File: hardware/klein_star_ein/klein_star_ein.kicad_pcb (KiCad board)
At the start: 2 copper layers, 1 part, among them U1 MT41K512M16

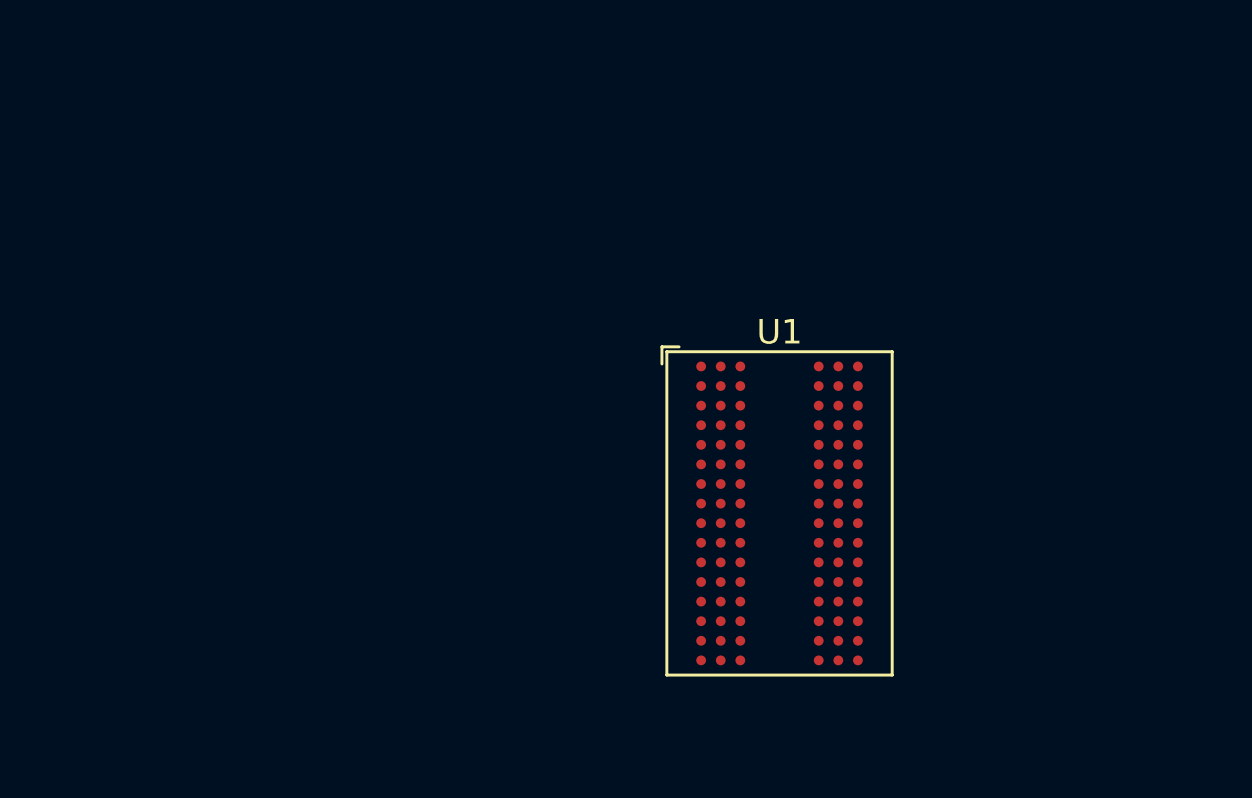
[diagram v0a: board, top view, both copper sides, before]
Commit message: fixed DRAM, added initial schematic
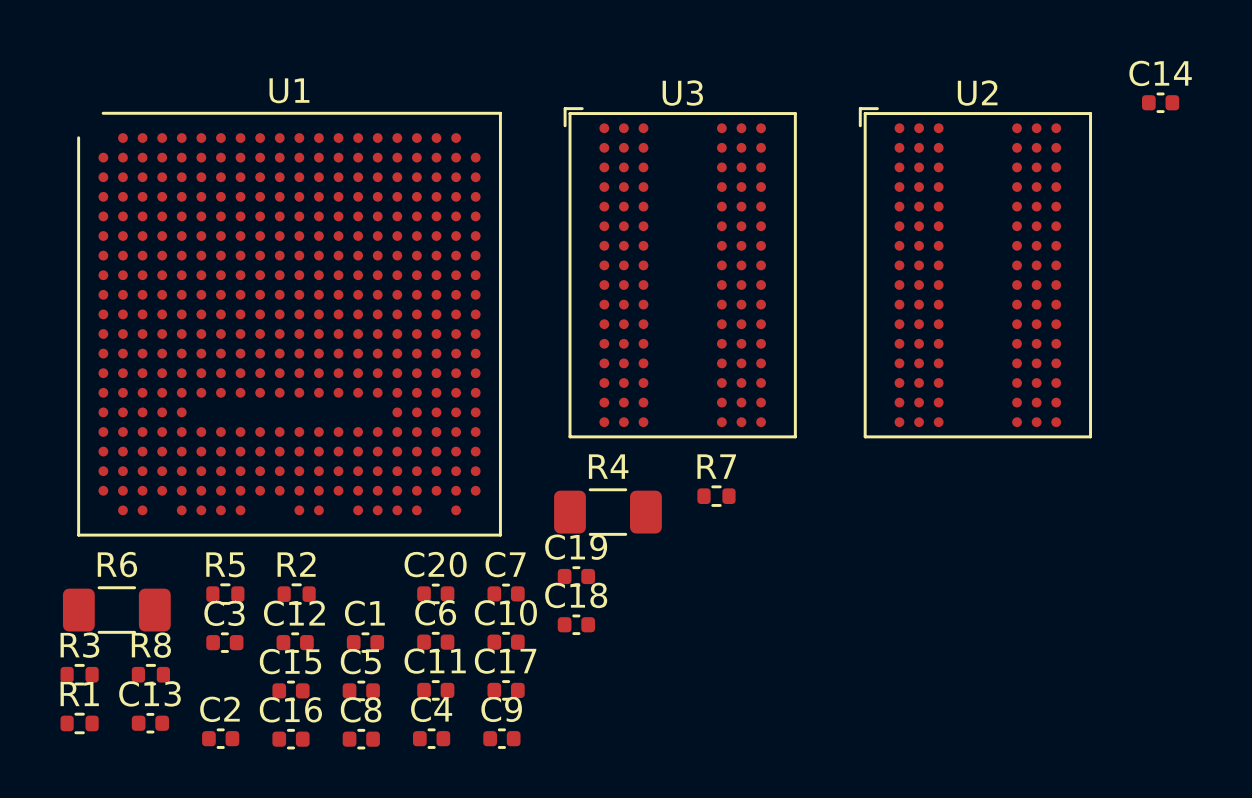
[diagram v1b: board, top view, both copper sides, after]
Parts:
- added C1: 0.1uF, Capacitor_SMD:C_0402_1005Metric, F.Cu at (140.8, 101.7)
- added C10: 0.1uF, Capacitor_SMD:C_0402_1005Metric, F.Cu at (146.5, 101.7)
- added C11: 0.1uF, Capacitor_SMD:C_0402_1005Metric, F.Cu at (143.6, 103.7)
- added C12: 0.1uF, Capacitor_SMD:C_0402_1005Metric, F.Cu at (137.9, 101.7)
- added C13: 4.7uF, Capacitor_SMD:C_0402_1005Metric, F.Cu at (132.0, 105.0)
- added C14: 0.1uF, Capacitor_SMD:C_0402_1005Metric, F.Cu at (173.2, 79.7)
- added C15: 0.1uF, Capacitor_SMD:C_0402_1005Metric, F.Cu at (137.7, 103.7)
- added C16: 4.7uF, Capacitor_SMD:C_0402_1005Metric, F.Cu at (137.7, 105.7)
- added C17: 0.1uF, Capacitor_SMD:C_0402_1005Metric, F.Cu at (146.5, 103.7)
- added C18: 0.1uF, Capacitor_SMD:C_0402_1005Metric, F.Cu at (149.4, 101.0)
- added C19: 0.1uF, Capacitor_SMD:C_0402_1005Metric, F.Cu at (149.4, 99.0)
- added C2: 0.1uF, Capacitor_SMD:C_0402_1005Metric, F.Cu at (134.9, 105.7)
- added C20: 0.1uF, Capacitor_SMD:C_0402_1005Metric, F.Cu at (143.6, 99.7)
- added C3: 0.1uF, Capacitor_SMD:C_0402_1005Metric, F.Cu at (135.0, 101.7)
- added C4: 0.1uF, Capacitor_SMD:C_0402_1005Metric, F.Cu at (143.5, 105.7)
- added C5: 0.1uF, Capacitor_SMD:C_0402_1005Metric, F.Cu at (140.6, 103.7)
- added C6: 4.7uF, Capacitor_SMD:C_0402_1005Metric, F.Cu at (143.6, 101.7)
- added C7: 0.1uF, Capacitor_SMD:C_0402_1005Metric, F.Cu at (146.5, 99.7)
- added C8: 4.7uF, Capacitor_SMD:C_0402_1005Metric, F.Cu at (140.6, 105.7)
- added C9: 0.1uF, Capacitor_SMD:C_0402_1005Metric, F.Cu at (146.3, 105.7)
- added R1: 51R, Resistor_SMD:R_0402_1005Metric, F.Cu at (129.1, 105.0)
- added R2: 51R, Resistor_SMD:R_0402_1005Metric, F.Cu at (138.0, 99.8)
- added R3: 240R, Resistor_SMD:R_0402_1005Metric, F.Cu at (129.1, 103.0)
- added R4: 0R, Resistor_SMD:R_1206_3216Metric_Pad1.30x1.75mm_HandSolder, F.Cu at (150.7, 96.4)
- added R5: 240R, Resistor_SMD:R_0402_1005Metric, F.Cu at (135.1, 99.8)
- added R6: 0R, Resistor_SMD:R_1206_3216Metric_Pad1.30x1.75mm_HandSolder, F.Cu at (130.6, 100.4)
- added R7: 51R, Resistor_SMD:R_0402_1005Metric, F.Cu at (155.1, 95.8)
- added R8: 51R, Resistor_SMD:R_0402_1005Metric, F.Cu at (132.0, 103.0)
- added U2: MT41K512M16, Package_BGA:BGA-96_9.0x13.0mm_Layout2x3x16_P0.8mm, F.Cu at (165.8, 86.7)
- added U3: MT41K512M16, Package_BGA:BGA-96_9.0x13.0mm_Layout2x3x16_P0.8mm, F.Cu at (153.7, 86.7)
- U1: value MT41K512M16 -> ECP5UM25; footprint Package_BGA:BGA-96_9.0x13.0mm_Layout2x3x16_P0.8mm -> Package_BGA:Lattice_caBGA-381_17.0x17.0mm_Layout20x20_P0.8mm_Ball0.4mm_Pad0.4mm_NSMD
- moved U1 21.4 mm to (137.7, 88.7)
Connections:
- net Net-(U1-PadB2) renamed /BANK_A_VREF
- net Net-(U1-PadC9) renamed no_connect_275
- net no_connect_93 renamed Net-(U1-PadJ1)
- net no_connect_95 renamed Net-(U1-PadL1)
- U1 pad A2: (no net) -> /BANK_A_DQ0
- U1 pad A3: Net-(U1-PadA3) -> /BANK_A_DQ10
- U1 pad B1: Net-(U1-PadB1) -> /BANK_A_DQ1
- U1 pad B3: Net-(U1-PadB3) -> /BANK_A_DQ11
- U1 pad B7: Net-(U1-PadB7) -> GND
- U1 pad C1: Net-(U1-PadC1) -> /BANK_A_DQ2
- U1 pad C2: Net-(U1-PadC2) -> /DRAM_A_nRESET
- U1 pad C3: Net-(U1-PadC3) -> /DRAM_A_CKE
- U1 pad D1: Net-(U1-PadD1) -> /BANK_A_DQ3
- U1 pad D2: Net-(U1-PadD2) -> /DRAM_A_nCS
- U1 pad D3: Net-(U1-PadD3) -> /DRAM_A_ODT
- U1 pad E1: Net-(U1-PadE1) -> /DRAM_A_nWE
- U1 pad E2: Net-(U1-PadE2) -> /BANK_A_DQ7
- U1 pad E3: Net-(U1-PadE3) -> /BANK_A_DQ13
- U1 pad F2: Net-(U1-PadF2) -> /BANK_A_DQ6
- U1 pad F3: Net-(U1-PadF3) -> /BANK_A_DQ5
- U1 pad F7: Net-(U1-PadF7) -> GND
- U1 pad F8: Net-(U1-PadF8) -> GND
- U1 pad G3: Net-(U1-PadG3) -> /BANK_A_DQ4
- U1 pad G7: Net-(U1-PadG7) -> GND
- U1 pad G8: Net-(U1-PadG8) -> GND
- U1 pad G9: Net-(U1-PadG9) -> GND
- U1 pad H3: Net-(U1-PadH3) -> /DRAM_A_LDM
- U1 pad J2: Net-(U1-PadJ2) -> GND
- U1 pad J7: Net-(U1-PadJ7) -> GND
- U1 pad J9: no_connect_94 -> GND
- U1 pad K7: Net-(U1-PadK7) -> GND
- U1 pad K9: Net-(U1-PadK9) -> GND
- U1 pad L9: no_connect_96 -> GND
- U1 pad M2: Net-(U1-PadM2) -> GND
- U1 pad M7: Net-(U1-PadM7) -> GND
- U1 pad M9: Net-(U1-PadM9) -> GND
- U1 pad N7: Net-(U1-PadN7) -> GND
- U1 pad P7: Net-(U1-PadP7) -> GND
- U1 pad P8: Net-(U1-PadP8) -> GND
- U1 pad P9: Net-(U1-PadP9) -> (no net)
- U1 pad R1: Net-(U1-PadR1) -> (no net)
- U1 pad R2: Net-(U1-PadR2) -> (no net)
- U1 pad R3: Net-(U1-PadR3) -> (no net)
- U1 pad T1: Net-(U1-PadT1) -> (no net)
- U1 pad T2: Net-(U1-PadT2) -> (no net)
- U1 pad T3: Net-(U1-PadT3) -> (no net)
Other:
- copper layers 2 -> 6

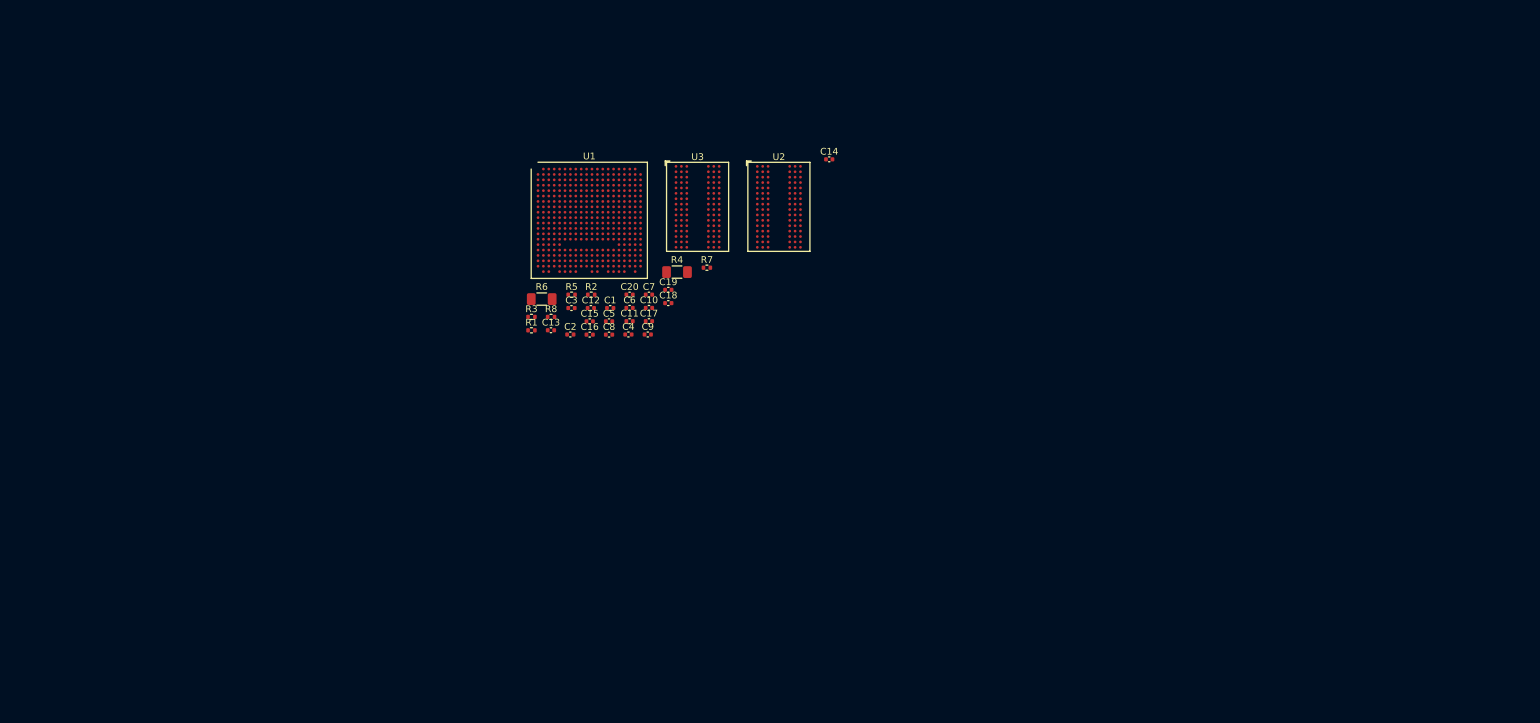
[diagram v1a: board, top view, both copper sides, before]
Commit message: changed RAM symbol, schematic of FT, USB PHY and VGA. Rerouted DRAM
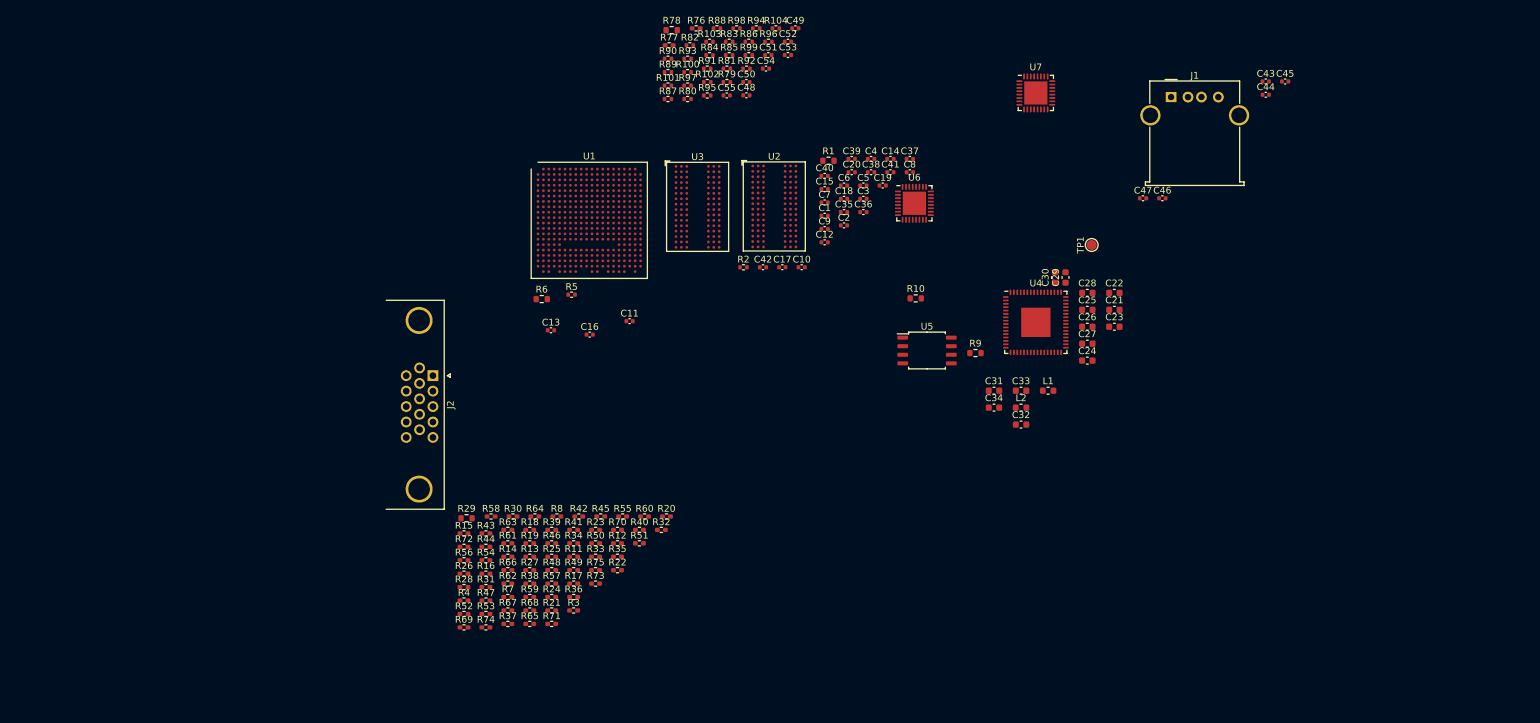
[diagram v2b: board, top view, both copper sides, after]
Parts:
- added C21: 100n, Capacitor_SMD:C_0603_1608Metric, F.Cu at (215.5, 102.0)
- added C22: 100n, Capacitor_SMD:C_0603_1608Metric, F.Cu at (215.5, 99.5)
- added C23: 100n, Capacitor_SMD:C_0603_1608Metric, F.Cu at (215.5, 104.5)
- added C24: 100n, Capacitor_SMD:C_0603_1608Metric, F.Cu at (211.5, 109.5)
- added C25: 100n, Capacitor_SMD:C_0603_1608Metric, F.Cu at (211.5, 102.0)
- added C26: 100n, Capacitor_SMD:C_0603_1608Metric, F.Cu at (211.5, 104.5)
- added C27: 100n, Capacitor_SMD:C_0603_1608Metric, F.Cu at (211.5, 107.0)
- added C28: 100n, Capacitor_SMD:C_0603_1608Metric, F.Cu at (211.5, 99.5)
- added C29: 100n, Capacitor_SMD:C_0603_1608Metric, F.Cu at (208.2, 97.2)
- added C30: 4u7, Capacitor_SMD:C_0603_1608Metric, F.Cu at (206.7, 97.2)
- added C31: 4u7, Capacitor_SMD:C_0603_1608Metric, F.Cu at (197.7, 114.0)
- added C32: 4u7, Capacitor_SMD:C_0603_1608Metric, F.Cu at (201.7, 119.0)
- added C33: 100n, Capacitor_SMD:C_0603_1608Metric, F.Cu at (201.7, 114.0)
- added C34: 100n, Capacitor_SMD:C_0603_1608Metric, F.Cu at (197.7, 116.5)
- added C35: 470n, Capacitor_SMD:C_0402_1005Metric, F.Cu at (175.4, 87.5)
- added C36: 470n, Capacitor_SMD:C_0402_1005Metric, F.Cu at (178.3, 87.5)
- added C37: 470n, Capacitor_SMD:C_0402_1005Metric, F.Cu at (185.2, 79.6)
- added C38: 470n, Capacitor_SMD:C_0402_1005Metric, F.Cu at (179.4, 81.6)
- added C39: 470n, Capacitor_SMD:C_0402_1005Metric, F.Cu at (176.6, 79.6)
- added C40: 100nF, Capacitor_SMD:C_0402_1005Metric, F.Cu at (172.6, 82.1)
- added C41: 100nF, Capacitor_SMD:C_0402_1005Metric, F.Cu at (182.3, 81.6)
- added C42: 100nF, Capacitor_SMD:C_0402_1005Metric, F.Cu at (163.4, 95.7)
- added C43: 100nF, Capacitor_SMD:C_0402_1005Metric, F.Cu at (237.9, 68.2)
- added C44: 100nF, Capacitor_SMD:C_0402_1005Metric, F.Cu at (237.9, 70.1)
- added C45: 100nF, Capacitor_SMD:C_0402_1005Metric, F.Cu at (240.8, 68.2)
- added C46: 100nF, Capacitor_SMD:C_0402_1005Metric, F.Cu at (222.6, 85.5)
- added C47: 4u7, Capacitor_SMD:C_0402_1005Metric, F.Cu at (219.7, 85.5)
- added C48: 100nF, Capacitor_SMD:C_0402_1005Metric, F.Cu at (160.9, 70.2)
- added C49: 100nF, Capacitor_SMD:C_0402_1005Metric, F.Cu at (168.2, 60.3)
- added C50: 100nF, Capacitor_SMD:C_0402_1005Metric, F.Cu at (160.9, 68.2)
- added C51: 100nF, Capacitor_SMD:C_0402_1005Metric, F.Cu at (164.2, 64.2)
- added C52: 4u7, Capacitor_SMD:C_0402_1005Metric, F.Cu at (167.1, 62.3)
- added C53: 100nF, Capacitor_SMD:C_0402_1005Metric, F.Cu at (167.1, 64.2)
- added C54: 100nF, Capacitor_SMD:C_0402_1005Metric, F.Cu at (163.9, 66.2)
- added C55: 100nF, Capacitor_SMD:C_0402_1005Metric, F.Cu at (158.0, 70.2)
- added J1: USB_A, Connector_USB:USB_A_Molex_67643_Horizontal, F.Cu at (223.9, 70.5)
- added J2: DB15_Female_HighDensity_MountingHoles, Connector_Dsub:DSUB-15-HD_Male_Horizontal_P2.29x1.98mm_EdgePinOffset3.03mm_Housed_MountingHolesOffset4.94mm, F.Cu at (114.5, 111.8)
- added L1: L_Small, Inductor_SMD:L_0603_1608Metric, F.Cu at (205.7, 114.0)
- added L2: L_Small, Inductor_SMD:L_0603_1608Metric, F.Cu at (201.7, 116.5)
- added R10: 12k +/-1%, Resistor_SMD:R_0603_1608Metric, F.Cu at (186.1, 100.3)
- added R100: 51R, Resistor_SMD:R_0402_1005Metric, F.Cu at (152.2, 66.8)
- added R101: 51R, Resistor_SMD:R_0402_1005Metric, F.Cu at (149.3, 68.8)
- added R102: 51R, Resistor_SMD:R_0402_1005Metric, F.Cu at (155.2, 68.2)
- added R103: 51R, Resistor_SMD:R_0402_1005Metric, F.Cu at (155.5, 62.3)
- added R104: 51R, Resistor_SMD:R_0402_1005Metric, F.Cu at (165.3, 60.3)
- added R11: R, Resistor_SMD:R_0402_1005Metric_Pad0.72x0.64mm_HandSolder, F.Cu at (135.3, 138.6)
- added R12: R, Resistor_SMD:R_0402_1005Metric_Pad0.72x0.64mm_HandSolder, F.Cu at (141.8, 136.6)
- added R13: R, Resistor_SMD:R_0402_1005Metric_Pad0.72x0.64mm_HandSolder, F.Cu at (128.8, 138.6)
- added R14: R, Resistor_SMD:R_0402_1005Metric_Pad0.72x0.64mm_HandSolder, F.Cu at (125.6, 138.6)
- added R15: R, Resistor_SMD:R_0402_1005Metric_Pad0.72x0.64mm_HandSolder, F.Cu at (119.1, 135.1)
- added R16: R, Resistor_SMD:R_0402_1005Metric_Pad0.72x0.64mm_HandSolder, F.Cu at (122.3, 141.1)
- added R17: R, Resistor_SMD:R_0402_1005Metric_Pad0.72x0.64mm_HandSolder, F.Cu at (135.3, 142.6)
- added R18: R, Resistor_SMD:R_0402_1005Metric_Pad0.72x0.64mm_HandSolder, F.Cu at (128.8, 134.6)
- added R19: R, Resistor_SMD:R_0402_1005Metric_Pad0.72x0.64mm_HandSolder, F.Cu at (128.8, 136.6)
- added R20: R, Resistor_SMD:R_0402_1005Metric_Pad0.72x0.64mm_HandSolder, F.Cu at (149.1, 132.6)
- added R21: R, Resistor_SMD:R_0402_1005Metric_Pad0.72x0.64mm_HandSolder, F.Cu at (132.1, 146.6)
- added R22: R, Resistor_SMD:R_0402_1005Metric_Pad0.72x0.64mm_HandSolder, F.Cu at (141.8, 140.6)
- added R23: R, Resistor_SMD:R_0402_1005Metric_Pad0.72x0.64mm_HandSolder, F.Cu at (138.6, 134.6)
- added R24: R, Resistor_SMD:R_0402_1005Metric_Pad0.72x0.64mm_HandSolder, F.Cu at (132.1, 144.6)
- added R25: R, Resistor_SMD:R_0402_1005Metric_Pad0.72x0.64mm_HandSolder, F.Cu at (132.1, 138.6)
- added R26: R, Resistor_SMD:R_0402_1005Metric_Pad0.72x0.64mm_HandSolder, F.Cu at (119.1, 141.1)
- added R27: R, Resistor_SMD:R_0402_1005Metric_Pad0.72x0.64mm_HandSolder, F.Cu at (128.8, 140.6)
- added R28: R, Resistor_SMD:R_0402_1005Metric_Pad0.72x0.64mm_HandSolder, F.Cu at (119.1, 143.1)
- added R29: 1M, Resistor_SMD:R_0603_1608Metric, F.Cu at (119.5, 132.9)
- added R30: R, Resistor_SMD:R_0402_1005Metric_Pad0.72x0.64mm_HandSolder, F.Cu at (126.4, 132.6)
- added R31: R, Resistor_SMD:R_0402_1005Metric_Pad0.72x0.64mm_HandSolder, F.Cu at (122.3, 143.1)
- added R32: R, Resistor_SMD:R_0402_1005Metric_Pad0.72x0.64mm_HandSolder, F.Cu at (148.3, 134.6)
- added R33: R, Resistor_SMD:R_0402_1005Metric_Pad0.72x0.64mm_HandSolder, F.Cu at (138.6, 138.6)
- added R34: R, Resistor_SMD:R_0402_1005Metric_Pad0.72x0.64mm_HandSolder, F.Cu at (135.3, 136.6)
- added R35: R, Resistor_SMD:R_0402_1005Metric_Pad0.72x0.64mm_HandSolder, F.Cu at (141.8, 138.6)
- added R36: R, Resistor_SMD:R_0402_1005Metric_Pad0.72x0.64mm_HandSolder, F.Cu at (135.3, 144.6)
- added R37: R, Resistor_SMD:R_0402_1005Metric_Pad0.72x0.64mm_HandSolder, F.Cu at (125.6, 148.5)
- added R38: R, Resistor_SMD:R_0402_1005Metric_Pad0.72x0.64mm_HandSolder, F.Cu at (128.8, 142.6)
- added R39: R, Resistor_SMD:R_0402_1005Metric_Pad0.72x0.64mm_HandSolder, F.Cu at (132.1, 134.6)
- added R40: R, Resistor_SMD:R_0402_1005Metric_Pad0.72x0.64mm_HandSolder, F.Cu at (145.1, 134.6)
- added R41: R, Resistor_SMD:R_0402_1005Metric_Pad0.72x0.64mm_HandSolder, F.Cu at (135.3, 134.6)
- added R42: R, Resistor_SMD:R_0402_1005Metric_Pad0.72x0.64mm_HandSolder, F.Cu at (136.1, 132.6)
- added R43: R, Resistor_SMD:R_0402_1005Metric_Pad0.72x0.64mm_HandSolder, F.Cu at (122.3, 135.1)
- added R44: 100R, Resistor_SMD:R_0402_1005Metric_Pad0.72x0.64mm_HandSolder, F.Cu at (122.3, 137.1)
- added R45: 100R, Resistor_SMD:R_0402_1005Metric_Pad0.72x0.64mm_HandSolder, F.Cu at (139.4, 132.6)
- added R46: R, Resistor_SMD:R_0402_1005Metric_Pad0.72x0.64mm_HandSolder, F.Cu at (132.1, 136.6)
- added R47: R, Resistor_SMD:R_0402_1005Metric_Pad0.72x0.64mm_HandSolder, F.Cu at (122.3, 145.1)
- added R48: R, Resistor_SMD:R_0402_1005Metric_Pad0.72x0.64mm_HandSolder, F.Cu at (132.1, 140.6)
- added R49: R, Resistor_SMD:R_0402_1005Metric_Pad0.72x0.64mm_HandSolder, F.Cu at (135.3, 140.6)
- added R50: R, Resistor_SMD:R_0402_1005Metric_Pad0.72x0.64mm_HandSolder, F.Cu at (138.6, 136.6)
- added R51: R, Resistor_SMD:R_0402_1005Metric_Pad0.72x0.64mm_HandSolder, F.Cu at (145.1, 136.6)
- added R52: R, Resistor_SMD:R_0402_1005Metric_Pad0.72x0.64mm_HandSolder, F.Cu at (119.1, 147.1)
- added R53: R, Resistor_SMD:R_0402_1005Metric_Pad0.72x0.64mm_HandSolder, F.Cu at (122.3, 147.1)
- added R54: R, Resistor_SMD:R_0402_1005Metric_Pad0.72x0.64mm_HandSolder, F.Cu at (122.3, 139.1)
- added R55: R, Resistor_SMD:R_0402_1005Metric_Pad0.72x0.64mm_HandSolder, F.Cu at (142.6, 132.6)
- added R56: R, Resistor_SMD:R_0402_1005Metric_Pad0.72x0.64mm_HandSolder, F.Cu at (119.1, 139.1)
- added R57: R, Resistor_SMD:R_0402_1005Metric_Pad0.72x0.64mm_HandSolder, F.Cu at (132.1, 142.6)
- added R58: R, Resistor_SMD:R_0402_1005Metric_Pad0.72x0.64mm_HandSolder, F.Cu at (123.1, 132.6)
- added R59: R, Resistor_SMD:R_0402_1005Metric_Pad0.72x0.64mm_HandSolder, F.Cu at (128.8, 144.6)
- added R60: R, Resistor_SMD:R_0402_1005Metric_Pad0.72x0.64mm_HandSolder, F.Cu at (145.9, 132.6)
- added R61: R, Resistor_SMD:R_0402_1005Metric_Pad0.72x0.64mm_HandSolder, F.Cu at (125.6, 136.6)
- added R62: R, Resistor_SMD:R_0402_1005Metric_Pad0.72x0.64mm_HandSolder, F.Cu at (125.6, 142.6)
- added R63: R, Resistor_SMD:R_0402_1005Metric_Pad0.72x0.64mm_HandSolder, F.Cu at (125.6, 134.6)
- added R64: R, Resistor_SMD:R_0402_1005Metric_Pad0.72x0.64mm_HandSolder, F.Cu at (129.6, 132.6)
- added R65: R, Resistor_SMD:R_0402_1005Metric_Pad0.72x0.64mm_HandSolder, F.Cu at (128.8, 148.5)
- added R66: R, Resistor_SMD:R_0402_1005Metric_Pad0.72x0.64mm_HandSolder, F.Cu at (125.6, 140.6)
- added R67: R, Resistor_SMD:R_0402_1005Metric_Pad0.72x0.64mm_HandSolder, F.Cu at (125.6, 146.6)
- added R68: R, Resistor_SMD:R_0402_1005Metric_Pad0.72x0.64mm_HandSolder, F.Cu at (128.8, 146.6)
- added R69: R, Resistor_SMD:R_0402_1005Metric_Pad0.72x0.64mm_HandSolder, F.Cu at (119.1, 149.1)
- added R70: R, Resistor_SMD:R_0402_1005Metric_Pad0.72x0.64mm_HandSolder, F.Cu at (141.8, 134.6)
- added R71: R, Resistor_SMD:R_0402_1005Metric_Pad0.72x0.64mm_HandSolder, F.Cu at (132.1, 148.5)
- added R72: R, Resistor_SMD:R_0402_1005Metric_Pad0.72x0.64mm_HandSolder, F.Cu at (119.1, 137.1)
- added R73: R, Resistor_SMD:R_0402_1005Metric_Pad0.72x0.64mm_HandSolder, F.Cu at (138.6, 142.6)
- added R74: R, Resistor_SMD:R_0402_1005Metric_Pad0.72x0.64mm_HandSolder, F.Cu at (122.3, 149.1)
- added R75: R, Resistor_SMD:R_0402_1005Metric_Pad0.72x0.64mm_HandSolder, F.Cu at (138.6, 140.6)
- added R76: 0R, Resistor_SMD:R_0402_1005Metric_Pad0.72x0.64mm_HandSolder, F.Cu at (153.5, 60.3)
- added R77: 0R, Resistor_SMD:R_0402_1005Metric_Pad0.72x0.64mm_HandSolder, F.Cu at (149.5, 62.8)
- added R78: 12k 1%, Resistor_SMD:R_0603_1608Metric, F.Cu at (149.9, 60.5)
- added R79: 51R, Resistor_SMD:R_0402_1005Metric, F.Cu at (158.1, 68.2)
- added R80: 51R, Resistor_SMD:R_0402_1005Metric, F.Cu at (152.2, 70.8)
- added R81: 51R, Resistor_SMD:R_0402_1005Metric, F.Cu at (158.1, 66.2)
- added R82: 51R, Resistor_SMD:R_0402_1005Metric, F.Cu at (152.6, 62.8)
- added R83: 51R, Resistor_SMD:R_0402_1005Metric, F.Cu at (158.4, 62.3)
- added R84: 51R, Resistor_SMD:R_0402_1005Metric, F.Cu at (155.5, 64.3)
- added R85: 51R, Resistor_SMD:R_0402_1005Metric, F.Cu at (158.4, 64.3)
- added R86: 51R, Resistor_SMD:R_0402_1005Metric, F.Cu at (161.3, 62.3)
- added R87: 51R, Resistor_SMD:R_0402_1005Metric, F.Cu at (149.3, 70.8)
- added R88: 51R, Resistor_SMD:R_0402_1005Metric, F.Cu at (156.6, 60.3)
- added R89: 51R, Resistor_SMD:R_0402_1005Metric, F.Cu at (149.3, 66.8)
- added R9: 10k, Resistor_SMD:R_0603_1608Metric, F.Cu at (194.9, 108.4)
- added R90: 51R, Resistor_SMD:R_0402_1005Metric, F.Cu at (149.3, 64.8)
- added R91: 51R, Resistor_SMD:R_0402_1005Metric, F.Cu at (155.2, 66.2)
- added R92: 51R, Resistor_SMD:R_0402_1005Metric, F.Cu at (161.0, 66.2)
- added R93: 51R, Resistor_SMD:R_0402_1005Metric, F.Cu at (152.2, 64.8)
- added R94: 51R, Resistor_SMD:R_0402_1005Metric, F.Cu at (162.4, 60.3)
- added R95: 51R, Resistor_SMD:R_0402_1005Metric, F.Cu at (155.2, 70.2)
- added R96: 51R, Resistor_SMD:R_0402_1005Metric, F.Cu at (164.2, 62.3)
- added R97: 51R, Resistor_SMD:R_0402_1005Metric, F.Cu at (152.2, 68.8)
- added R98: 51R, Resistor_SMD:R_0402_1005Metric, F.Cu at (159.5, 60.3)
- added R99: 51R, Resistor_SMD:R_0402_1005Metric, F.Cu at (161.3, 64.3)
- added TP1: FTDI1V8REG, TestPoint:TestPoint_Pad_D1.5mm, F.Cu at (212.1, 92.4)
- added U4: FT2232HQ, Package_DFN_QFN:QFN-64-1EP_9x9mm_P0.5mm_EP4.35x4.35mm, F.Cu at (203.8, 103.8)
- added U5: W25Q128JVS, Package_SO:SOIC-8_5.23x5.23mm_P1.27mm, F.Cu at (187.7, 108.0)
- added U6: USB3300-EZK, Package_DFN_QFN:QFN-32-1EP_5x5mm_P0.5mm_EP3.45x3.45mm, F.Cu at (185.8, 86.2)
- added U7: USB3300-EZK, Package_DFN_QFN:QFN-32-1EP_5x5mm_P0.5mm_EP3.45x3.45mm, F.Cu at (203.8, 69.8)
- C1: value 0.1uF -> 4.7uF
- C10, C12, C14, C15, C17, C18, C19, C2, C20, C3, C4, C5, C7, C9: value 0.1uF -> 470n
- C11: value 0.1uF -> 100nF
- C16, C6, C8: value 4.7uF -> 470n
- R1: value 51R -> 0R; footprint Resistor_SMD:R_0402_1005Metric -> Resistor_SMD:R_0603_1608Metric
- R2: value 51R -> 240R
- R3: value 240R -> R; footprint Resistor_SMD:R_0402_1005Metric -> Resistor_SMD:R_0402_1005Metric_Pad0.72x0.64mm_HandSolder
- R4: value 0R -> R; footprint Resistor_SMD:R_1206_3216Metric_Pad1.30x1.75mm_HandSolder -> Resistor_SMD:R_0402_1005Metric_Pad0.72x0.64mm_HandSolder
- R6: footprint Resistor_SMD:R_1206_3216Metric_Pad1.30x1.75mm_HandSolder -> Resistor_SMD:R_0603_1608Metric
- R7, R8: value 51R -> R; footprint Resistor_SMD:R_0402_1005Metric -> Resistor_SMD:R_0402_1005Metric_Pad0.72x0.64mm_HandSolder
- moved R4 58.0 mm to (119.1, 145.1)
- moved R7 57.0 mm to (125.6, 144.6)
- moved R1 50.7 mm to (173.1, 79.9)
- moved C8 50.7 mm to (185.2, 81.6)
- moved C3 46.2 mm to (178.3, 85.5)
- moved C4 44.4 mm to (179.4, 79.6)
- moved R3 44.0 mm to (135.3, 146.6)
- moved C2 43.7 mm to (175.4, 89.5)
- moved C5 42.7 mm to (178.3, 83.6)
- moved C15 40.0 mm to (172.6, 84.1)
- moved C20 37.6 mm to (176.6, 81.6)
- moved C6 36.6 mm to (175.4, 83.6)
- moved C12 36.0 mm to (172.6, 92.0)
- moved C19 35.3 mm to (181.2, 83.6)
- moved C1 34.6 mm to (172.6, 88.0)
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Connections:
- net /BANK_A_VREF renamed Net-(U1-PadB2)
- net /BANK_B_VREF renamed Net-(U1-PadD20)
- net no_connect_274 renamed no_connect_466
- net no_connect_275 renamed no_connect_467
- net no_connect_276 renamed no_connect_468
- net no_connect_277 renamed no_connect_469
- net no_connect_278 renamed no_connect_470
- net no_connect_279 renamed no_connect_471
- net no_connect_280 renamed no_connect_472
- net no_connect_281 renamed no_connect_473
- net no_connect_282 renamed no_connect_474
- net no_connect_283 renamed no_connect_475
- net no_connect_284 renamed no_connect_476
- net no_connect_285 renamed no_connect_477
- net no_connect_286 renamed no_connect_478
- net no_connect_287 renamed no_connect_479
- net no_connect_288 renamed no_connect_480
- net no_connect_289 renamed no_connect_481
- net no_connect_290 renamed no_connect_482
- net no_connect_291 renamed no_connect_483
- net no_connect_292 renamed no_connect_484
- net no_connect_293 renamed no_connect_485
- net no_connect_294 renamed no_connect_486
- net no_connect_295 renamed no_connect_487
- net no_connect_296 renamed no_connect_488
- net no_connect_297 renamed no_connect_489
- net no_connect_298 renamed no_connect_490
- net no_connect_299 renamed no_connect_491
- net no_connect_300 renamed no_connect_492
- net no_connect_301 renamed no_connect_493
- net no_connect_302 renamed no_connect_494
- net no_connect_303 renamed no_connect_495
- net no_connect_304 renamed no_connect_496
- net no_connect_305 renamed no_connect_497
- net no_connect_306 renamed no_connect_498
- net no_connect_307 renamed no_connect_499
- C1 pad 1: /DRAMREF -> Net-(C1-Pad1)
- C10 pad 1: /DRAM_SUPPLY_B -> Net-(U3-PadB2)
- C11 pad 1: /DRAMREF -> DRAM_VREF
- C12 pad 1: /DRAM_SUPPLY_A -> Net-(C1-Pad1)
- C13 pad 1: /DRAM_SUPPLY_A -> Net-(U3-PadB2)
- C14 pad 1: /DRAMREF -> Net-(U3-PadB2)
- C15 pad 1: /DRAM_SUPPLY_A -> Net-(C1-Pad1)
- C16 pad 1: /DRAM_SUPPLY_A -> Net-(U3-PadB2)
- C17 pad 1: /DRAMREF -> Net-(U3-PadB2)
- C18 pad 1: /DRAM_SUPPLY_A -> Net-(C1-Pad1)
- C19 pad 1: /DRAM_SUPPLY_A -> Net-(U3-PadB2)
- C2 pad 1: /DRAMREF -> Net-(C1-Pad1)
- C20 pad 1: Net-(C20-Pad1) -> Net-(C1-Pad1)
- C3 pad 1: /DRAMREF -> Net-(C1-Pad1)
- C4 pad 1: Net-(C4-Pad1) -> Net-(U3-PadB2)
- C5 pad 1: /DRAM_SUPPLY_B -> Net-(C1-Pad1)
- C6 pad 1: /DRAM_SUPPLY_B -> Net-(U3-PadB2)
- C7 pad 1: /DRAM_SUPPLY_B -> Net-(C1-Pad1)
- C8 pad 1: /DRAM_SUPPLY_B -> Net-(U3-PadB2)
- C9 pad 1: /DRAM_SUPPLY_B -> Net-(C1-Pad1)
- R1 pad 1: /DRAM_B_CK_P -> Net-(C1-Pad1)
- R1 pad 2: Net-(C4-Pad1) -> +1V35
- R2 pad 1: /DRAM_B_CK_N -> Net-(R2-Pad1)
- R2 pad 2: Net-(C4-Pad1) -> GND
- R3 pad 1: Net-(R3-Pad1) -> /VGA_BUF_R_0
- R3 pad 2: GND -> Net-(R14-Pad1)
- R4 pad 1: /DRAM_SUPPLY_GLOB -> /VGA_BUF_R_1
- R4 pad 2: /DRAM_SUPPLY_B -> Net-(R15-Pad1)
- R6 pad 1: /DRAM_SUPPLY_GLOB -> Net-(U3-PadB2)
- R6 pad 2: /DRAM_SUPPLY_A -> +1V35
- R7 pad 1: /DRAM_A_CK_P -> /VGA_BUF_R_2
- R7 pad 2: Net-(C20-Pad1) -> Net-(R16-Pad1)
- R8 pad 1: /DRAM_A_CK_N -> /VGA_BUF_R_3
- R8 pad 2: Net-(C20-Pad1) -> Net-(R17-Pad1)
- U1 pad A11: Net-(U1-PadA11) -> Net-(U1-PadA10)
- U1 pad A2: /BANK_A_DQ0 -> Net-(U1-PadA2)
- U1 pad A3: /BANK_A_DQ10 -> Net-(U1-PadA3)
- U1 pad A4: /DRAM_A_CK_N -> Net-(U1-PadA4)
- U1 pad A5: /DRAM_A_CK_P -> Net-(U1-PadA5)
- U1 pad A6: Net-(U1-PadA6) -> Net-(U1-PadA10)
- U1 pad A7: Net-(U1-PadA7) -> Net-(U1-PadA10)
- U1 pad A8: Net-(U1-PadA8) -> Net-(U1-PadA10)
- U1 pad A9: Net-(U1-PadA9) -> Net-(U1-PadA10)
- U1 pad B1: /BANK_A_DQ1 -> Net-(U1-PadB1)
- U1 pad B10: Net-(U1-PadB10) -> Net-(U1-PadA10)
- U1 pad B11: Net-(U1-PadB11) -> Net-(U1-PadA10)
- U1 pad B3: /BANK_A_DQ11 -> Net-(U1-PadB3)
- U1 pad B4: /BANK_A_DQ9 -> Net-(U1-PadB4)
- U1 pad B5: /DRAM_A_nCAS -> Net-(U1-PadB5)
- U1 pad B6: Net-(U1-PadB6) -> Net-(U1-PadA10)
- U1 pad B8: Net-(U1-PadB8) -> Net-(U1-PadA10)
- U1 pad B9: Net-(U1-PadB9) -> Net-(U1-PadA10)
- U1 pad C1: /BANK_A_DQ2 -> Net-(U1-PadC1)
- U1 pad C10: Net-(U1-PadC10) -> Net-(U1-PadA10)
- U1 pad C11: Net-(U1-PadC11) -> Net-(U1-PadA10)
- U1 pad C18: /DRAM_B_CK_N -> Net-(U1-PadC18)
- U1 pad C2: /DRAM_A_nRESET -> Net-(U1-PadC2)
- U1 pad C20: /BANK_B_DQ0 -> Net-(U1-PadC20)
- U1 pad C3: /DRAM_A_CKE -> Net-(U1-PadC3)
- U1 pad C4: /BANK_A_DQ8 -> Net-(U1-PadC4)
- U1 pad C5: /DRAM_A_nRAS -> Net-(U1-PadC5)
- U1 pad C6: Net-(U1-PadC6) -> Net-(U1-PadA10)
- U1 pad C7: Net-(U1-PadC7) -> Net-(U1-PadA10)
- U1 pad C8: Net-(U1-PadC8) -> Net-(U1-PadA10)
- U1 pad D1: /BANK_A_DQ3 -> Net-(U1-PadD1)
- U1 pad D17: /DRAM_B_CK_P -> Net-(U1-PadD17)
- U1 pad D18: /BANK_B_DQ8 -> Net-(U1-PadD18)
- U1 pad D19: /BANK_B_DQ1 -> Net-(U1-PadD19)
- U1 pad D2: /DRAM_A_nCS -> Net-(U1-PadD2)
- U1 pad D3: /DRAM_A_ODT -> Net-(U1-PadD3)
- U1 pad D5: /BANK_AH_RDQSN -> Net-(U1-PadD5)
- U1 pad D6: Net-(U1-PadD6) -> Net-(U1-PadA10)
- U1 pad D7: Net-(U1-PadD7) -> Net-(U1-PadA10)
- U1 pad D8: Net-(U1-PadD8) -> Net-(U1-PadA10)
- U1 pad D9: Net-(U1-PadD9) -> Net-(U1-PadA10)
- U1 pad E1: /DRAM_A_nWE -> Net-(U1-PadE1)
- U1 pad E16: /DRAM_B_nCAS -> Net-(U1-PadE16)
- U1 pad E17: /BANK_B_DQ9 -> Net-(U1-PadE17)
- U1 pad E18: /BANK_B_DQ10 -> Net-(U1-PadE18)
- U1 pad E19: /DRAM_B_nRESET -> Net-(U1-PadE19)
- U1 pad E2: /BANK_A_DQ7 -> Net-(U1-PadE2)
- U1 pad E20: /BANK_B_DQ2 -> Net-(U1-PadE20)
- U1 pad E3: /BANK_A_DQ13 -> Net-(U1-PadE3)
- U1 pad E4: /BANK_AH_RDQS -> Net-(U1-PadE4)
- U1 pad E5: /BANK_A_DQ14 -> Net-(U1-PadE5)
- U1 pad E6: Net-(U1-PadE6) -> Net-(U1-PadA10)
- U1 pad E7: Net-(U1-PadE7) -> Net-(U1-PadA10)
- U1 pad E8: Net-(U1-PadE8) -> Net-(U1-PadA10)
- U1 pad E9: Net-(U1-PadE9) -> Net-(U1-PadA10)
- U1 pad F16: /DRAM_B_nRAS -> Net-(U1-PadF16)
- U1 pad F17: /BANK_BH_RDQS -> Net-(U1-PadF17)
- U1 pad F18: /BANK_B_DQ11 -> Net-(U1-PadF18)
- U1 pad F19: /BANK_B_DQ3 -> Net-(U1-PadF19)
- U1 pad F2: /BANK_A_DQ6 -> Net-(U1-PadF2)
- U1 pad F20: /DRAM_B_nCS -> Net-(U1-PadF20)
- U1 pad F3: /BANK_A_DQ5 -> Net-(U1-PadF3)
- U1 pad F4: /BANK_A_DQ12 -> Net-(U1-PadF4)
- U1 pad F5: /BANK_A_DQ15 -> Net-(U1-PadF5)
- U1 pad G16: /DRAM_B_CKE -> Net-(U1-PadG16)
- U1 pad G18: /BANK_BH_RDQSN -> Net-(U1-PadG18)
- U1 pad G19: /BANK_BL_RDQS -> Net-(U1-PadG19)
- U1 pad G20: /DRAM_B_nWE -> Net-(U1-PadG20)
- U1 pad G3: /BANK_A_DQ4 -> Net-(U1-PadG3)
- U1 pad G5: /BANK_AL_RDQSN -> Net-(U1-PadG5)
- U1 pad H14: /DRAM_SUPPLY_GLOB -> Net-(U1-PadH14)
- U1 pad H15: /DRAM_SUPPLY_GLOB -> Net-(U1-PadH15)
- U1 pad H16: /DRAM_B_ODT -> Net-(U1-PadH16)
- U1 pad H17: /BANK_B_DQ13 -> Net-(U1-PadH17)
- U1 pad H18: /BANK_B_DQ12 -> Net-(U1-PadH18)
- U1 pad H20: /BANK_BL_RDQSN -> Net-(U1-PadH20)
- U1 pad H3: /DRAM_A_LDM -> Net-(U1-PadH3)
- U1 pad H4: /BANK_AL_RDQS -> Net-(U1-PadH4)
- U1 pad H5: /DRAM_A_UDM -> Net-(U1-PadH5)
- U1 pad J15: /DRAM_SUPPLY_GLOB -> Net-(U1-PadJ15)
- U1 pad J16: /BANK_B_DQ15 -> Net-(U1-PadJ16)
- U1 pad J17: /BANK_B_DQ14 -> Net-(U1-PadJ17)
- U1 pad J18: /DRAM_B_UDM -> Net-(U1-PadJ18)
- U1 pad J19: /BANK_B_DQ4 -> Net-(U1-PadJ19)
- U1 pad J20: /BANK_B_DQ6 -> Net-(U1-PadJ20)
- U1 pad K18: /DRAM_B_LDM -> Net-(U1-PadK18)
- U1 pad K19: /BANK_B_DQ5 -> Net-(U1-PadK19)
- U1 pad K20: /BANK_B_DQ7 -> Net-(U1-PadK20)
- U2 pad A1: /DRAM_SUPPLY_B -> Net-(C1-Pad1)
- U2 pad A2: /BANK_B_DQ13 -> /DRAM_DATA_13
- U2 pad A3: /BANK_B_DQ15 -> /DRAM_DATA_15
- U2 pad A7: /BANK_B_DQ12 -> /DRAM_DATA_12
- U2 pad A8: /DRAM_SUPPLY_B -> Net-(C1-Pad1)
- U2 pad B2: /DRAM_SUPPLY_B -> Net-(C1-Pad1)
- U2 pad B7: /BANK_BH_RDQSN -> /DRAM_DQS1_N
- U2 pad B8: /BANK_B_DQ14 -> /DRAM_DATA_14
- U2 pad C1: /DRAM_SUPPLY_B -> Net-(C1-Pad1)
- U2 pad C2: /BANK_B_DQ11 -> /DRAM_DATA_11
- U2 pad C3: /BANK_B_DQ9 -> /DRAM_DATA_9
- U2 pad C7: /BANK_BH_RDQS -> /DRAM_DQS1_P
- U2 pad C8: /BANK_B_DQ10 -> /DRAM_DATA_10
- U2 pad C9: /DRAM_SUPPLY_B -> Net-(C1-Pad1)
- U2 pad D2: /DRAM_SUPPLY_B -> Net-(C1-Pad1)
- U2 pad D3: /DRAM_B_UDM -> /DRAM_DM1
- U2 pad D7: /BANK_B_DQ8 -> /DRAM_DATA_8
- U2 pad D9: /DRAM_SUPPLY_B -> Net-(C1-Pad1)
- U2 pad E3: /BANK_B_DQ0 -> /DRAM_DATA_0
- U2 pad E7: /DRAM_B_LDM -> /DRAM_DM0
- U2 pad E9: /DRAM_SUPPLY_B -> Net-(C1-Pad1)
- U2 pad F1: /DRAM_SUPPLY_B -> Net-(C1-Pad1)
- U2 pad F2: /BANK_B_DQ2 -> /DRAM_DATA_2
- U2 pad F3: /BANK_BL_RDQS -> /DRAM_DQS0_P
- U2 pad F7: /BANK_B_DQ1 -> /DRAM_DATA_1
- U2 pad F8: /BANK_B_DQ3 -> /DRAM_DATA_3
- U2 pad G2: /BANK_B_DQ6 -> /DRAM_DATA_6
- U2 pad G3: /BANK_BL_RDQSN -> /DRAM_DQS0_N
- U2 pad G7: /DRAM_SUPPLY_B -> Net-(C1-Pad1)
- U2 pad H1: /DRAMREF -> DRAM_VREF
- U2 pad H2: /DRAM_SUPPLY_B -> Net-(C1-Pad1)
- U2 pad H3: /BANK_B_DQ4 -> /DRAM_DATA_4
- U2 pad H7: /BANK_B_DQ7 -> /DRAM_DATA_7
- U2 pad H8: /BANK_B_DQ5 -> /DRAM_DATA_5
- U2 pad H9: /DRAM_SUPPLY_B -> Net-(C1-Pad1)
- U2 pad J3: /DRAM_B_nRAS -> /DRAM_nRAS
- U2 pad J7: /DRAM_B_CK_P -> /DRAM_CLK_P
- U2 pad K1: /DRAM_B_ODT -> /DRAM_ODT
- U2 pad K2: /DRAM_SUPPLY_B -> Net-(C1-Pad1)
- U2 pad K3: /DRAM_B_nCAS -> /DRAM_nCAS
- U2 pad K7: /DRAM_B_CK_N -> /DRAM_CLK_N
- U2 pad K8: /DRAM_SUPPLY_B -> Net-(C1-Pad1)
- U2 pad K9: /DRAM_B_CKE -> /DRAM_CKE
- U2 pad L2: /DRAM_B_nCS -> /DRAM_nCS
- U2 pad L3: /DRAM_B_nWE -> /DRAM_nWE
- U2 pad L8: Net-(R3-Pad1) -> Net-(R2-Pad1)
- U2 pad M8: /DRAMREF -> DRAM_VREF
- U2 pad N1: /DRAM_SUPPLY_B -> Net-(C1-Pad1)
- U2 pad N9: /DRAM_SUPPLY_B -> Net-(C1-Pad1)
- U2 pad R1: /DRAM_SUPPLY_B -> Net-(C1-Pad1)
- U2 pad R9: /DRAM_SUPPLY_B -> Net-(C1-Pad1)
- U2 pad T2: /DRAM_B_nRESET -> /DRAM_nRESET
- U3 pad A1: /DRAM_SUPPLY_A -> Net-(U3-PadB2)
- U3 pad A2: /BANK_A_DQ13 -> /DRAM_DATA_29
- U3 pad A3: /BANK_A_DQ15 -> /DRAM_DATA_31
- U3 pad A7: /BANK_A_DQ12 -> /DRAM_DATA_28
- U3 pad A8: /DRAM_SUPPLY_A -> Net-(U3-PadB2)
- U3 pad B2: /DRAM_SUPPLY_A -> Net-(U3-PadB2)
- U3 pad B7: /BANK_AH_RDQSN -> /DRAM_DQS3_N
- U3 pad B8: /BANK_A_DQ14 -> /DRAM_DATA_30
- U3 pad C1: /DRAM_SUPPLY_A -> Net-(U3-PadB2)
- U3 pad C2: /BANK_A_DQ11 -> /DRAM_DATA_27
- U3 pad C3: /BANK_A_DQ9 -> /DRAM_DATA_25
- U3 pad C7: /BANK_AH_RDQS -> /DRAM_DQS3_P
- U3 pad C8: /BANK_A_DQ10 -> /DRAM_DATA_26
- U3 pad C9: /DRAM_SUPPLY_A -> Net-(U3-PadB2)
- U3 pad D2: /DRAM_SUPPLY_A -> Net-(U3-PadB2)
- U3 pad D3: /DRAM_A_UDM -> /DRAM_DM3
- U3 pad D7: /BANK_A_DQ8 -> /DRAM_DATA_24
- U3 pad D9: /DRAM_SUPPLY_A -> Net-(U3-PadB2)
- U3 pad E3: /BANK_A_DQ0 -> /DRAM_DATA_16
- U3 pad E7: /DRAM_A_LDM -> /DRAM_DM2
- U3 pad E9: /DRAM_SUPPLY_A -> Net-(U3-PadB2)
- U3 pad F1: /DRAM_SUPPLY_A -> Net-(U3-PadB2)
- U3 pad F2: /BANK_A_DQ2 -> /DRAM_DATA_18
- U3 pad F3: /BANK_AL_RDQS -> /DRAM_DQS2_P
- U3 pad F7: /BANK_A_DQ1 -> /DRAM_DATA_17
- U3 pad F8: /BANK_A_DQ3 -> /DRAM_DATA_19
- U3 pad G2: /BANK_A_DQ6 -> /DRAM_DATA_22
- U3 pad G3: /BANK_AL_RDQSN -> /DRAM_DQS2_N
- U3 pad G7: /DRAM_SUPPLY_A -> Net-(U3-PadB2)
- U3 pad H1: /DRAMREF -> DRAM_VREF
- U3 pad H2: /DRAM_SUPPLY_A -> Net-(U3-PadB2)
- U3 pad H3: /BANK_A_DQ4 -> /DRAM_DATA_20
- U3 pad H7: /BANK_A_DQ7 -> /DRAM_DATA_23
- U3 pad H8: /BANK_A_DQ5 -> /DRAM_DATA_21
- U3 pad H9: /DRAM_SUPPLY_A -> Net-(U3-PadB2)
- U3 pad J3: /DRAM_A_nRAS -> /DRAM_nRAS
- U3 pad J7: /DRAM_A_CK_P -> /DRAM_CLK_P
- U3 pad K1: /DRAM_A_ODT -> /DRAM_ODT
- U3 pad K2: /DRAM_SUPPLY_A -> Net-(U3-PadB2)
- U3 pad K3: /DRAM_A_nCAS -> /DRAM_nCAS
- U3 pad K7: /DRAM_A_CK_N -> /DRAM_CLK_N
- U3 pad K8: /DRAM_SUPPLY_A -> Net-(U3-PadB2)
- U3 pad K9: /DRAM_A_CKE -> /DRAM_CKE
- U3 pad L2: /DRAM_A_nCS -> /DRAM_nCS
- U3 pad L3: /DRAM_A_nWE -> /DRAM_nWE
- U3 pad M8: /DRAMREF -> DRAM_VREF
- U3 pad N1: /DRAM_SUPPLY_A -> Net-(U3-PadB2)
- U3 pad N9: /DRAM_SUPPLY_A -> Net-(U3-PadB2)
- U3 pad R1: /DRAM_SUPPLY_A -> Net-(U3-PadB2)
- U3 pad R9: /DRAM_SUPPLY_A -> Net-(U3-PadB2)
- U3 pad T2: /DRAM_A_nRESET -> /DRAM_nRESET
